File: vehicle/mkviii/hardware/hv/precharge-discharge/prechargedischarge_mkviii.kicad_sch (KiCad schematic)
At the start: 87 parts, among them J2 Conn_01x03_Pin, J3 CONN_pcie_x1, J4 Conn_01x03_Pin, K1 G2RG-2A-X_DC12, K2 3350-4275-126, K3 G2RG-2A-X_DC12, Q1 SSM3K333R, Q2 SSM3K333R, U1 U_GATE_SN74LVC1G02DBVR, U10 SN74LVC1G08DBVR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

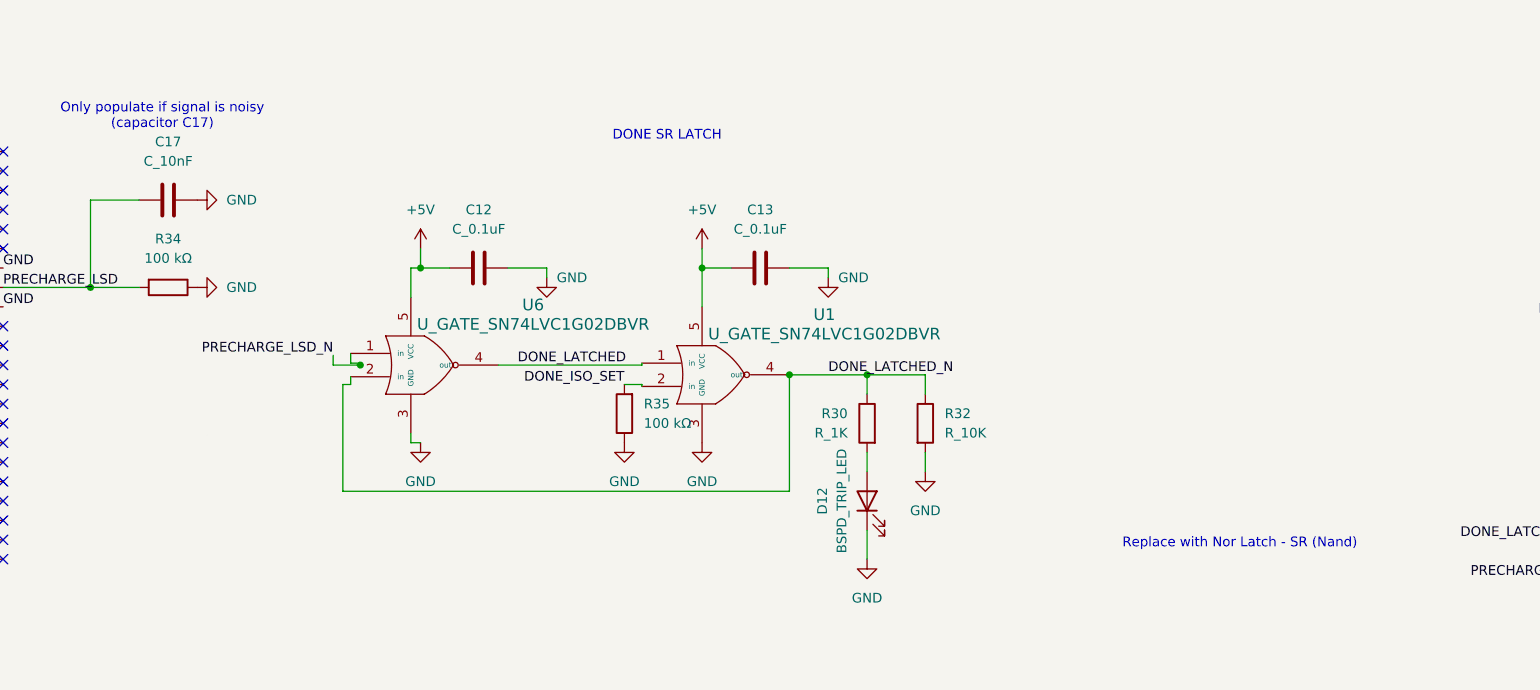
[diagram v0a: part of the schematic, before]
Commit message: Added Production Files; corrected various things in silkscreen and schematics
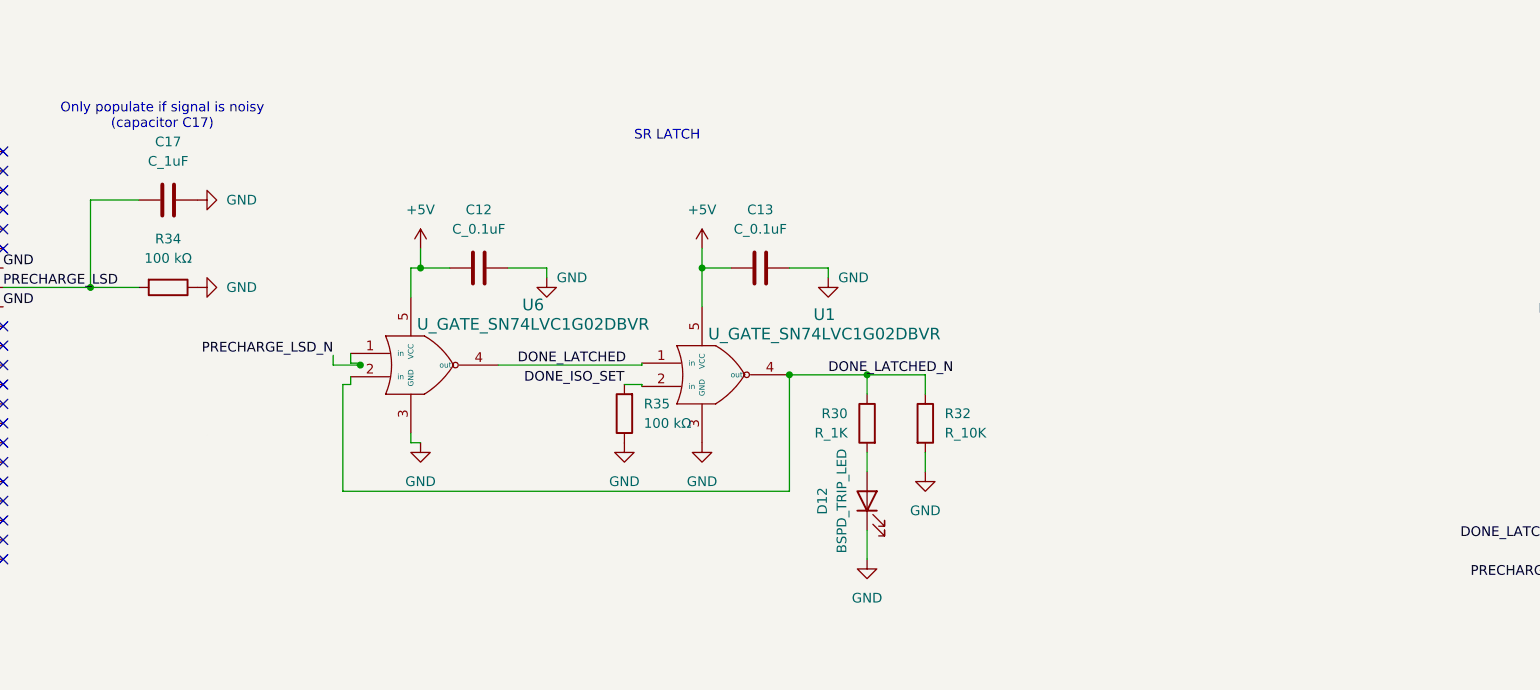
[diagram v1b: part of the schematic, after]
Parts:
- C17: value C_10nF -> C_1uF
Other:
- note added: "SR LATCH"
- note removed: "DONE SR LATCH"
- note removed: "Replace with Nor Latch - SR (Nand)"
- title: (none) -> Precharge-Discharge

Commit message: Prechrarge Discharge - Schematic Organized
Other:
- note added: "HV"
- note added: "LV"
- note added: "Latch Reset"
- note added: "OPTOCOUPLER Isolation"
- note added: "Precharge Completion Comparator"
- note added: "Precharge Done Logic"
- note added: "Precharge Relays"
- note added: "Status Indicator LED"
- note added: "Voltage Divider Network"
- note removed: "OPTOCOUPLER"
- note removed: "Precharge Relay"
- moved on the sheet: C1, C10, C11, C12, C13, C14, C15, C16, C17, C2, C3, C4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

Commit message: Precharge-discharge Renaming for BOM
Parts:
- C11: value C_2.2uF_25V -> C_2.2uF
- C12, C13: value C_0.1uF -> 0.1 µF
- D10, D13: footprint LED_SMD:LED_0805_2012Metric -> OEM:D_0805_2012Metric
- D12: value BSPD_TRIP_LED -> LED_WHITE
- D7, D9: footprint Diode_SMD:D_SMA -> OEM:D_SOD-128
- R1: value 10KR -> R_10K; footprint OEM:R_0603 -> OEM:R_0603_1608Metric
- R11, R5, R7, R8: footprint OEM:R_0603 -> OEM:R_0603_1608Metric
- R24, R27, R30: value R_1K -> 1KR
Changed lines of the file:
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@@
 			)
 		)
-		(property "Footprint" "OEM:R_0603"
+		(property "Footprint" "OEM:R_0603_1608Metric"
 			(at 68.58 191.008 0)
 			(effects
@@
 		)
 		(instances
-			(project "precharge_discharge"
+			(project "prechargedischarge_mkviii"
 				(path "/96f56455-bf31-456c-8371-5b3706690d23"
 					(reference "R8")
@@
 		)
 		(instances
-			(project ""
+			(project "prechargedischarge_mkviii"
 				(path "/96f56455-bf31-456c-8371-5b3706690d23"
 					(reference "U5")
@@
 		)
 		(instances
-			(project "precharge_discharge"
+			(project "prechargedischarge_mkviii"
 				(path "/96f56455-bf31-456c-8371-5b3706690d23"
 					(reference "K1")
@@
 			)
 		)
-		(property "Footprint" "OEM:R_0603"
+		(property "Footprint" "OEM:R_0603_1608Metric"
 			(at 240.03 191.008 90)
 			(effects
@@
 		)
 		(instances
-			(project "precharge_discharge"
+			(project "prechargedischarge_mkviii"
 				(path "/96f56455-bf31-456c-8371-5b3706690d23"
 					(reference "R5")
@@
 			)
 		)
-		(property "Value" "C_0.1uF"
+		(property "Value" "0.1 µF"
 			(at 347.98 54.61 90)
 			(effects
@@
 		)
 		(instances
-			(project ""
+			(project "prechargedischarge_mkviii"
 				(path "/96f56455-bf31-456c-8371-5b3706690d23"
 					(reference "R15")
@@
 		)
 		(instances
-			(project "precharge_discharge"
+			(project "prechargedischarge_mkviii"
 				(path "/96f56455-bf31-456c-8371-5b3706690d23"
 					(reference "J4")
@@
 		)
 		(instances
-			(project "precharge_discharge"
+			(project "prechargedischarge_mkviii"
 				(path "/96f56455-bf31-456c-8371-5b3706690d23"
 					(reference "D1")
@@
 		)
 		(instances
-			(project "precharge_discharge"
+			(project "prechargedischarge_mkviii"
 				(path "/96f56455-bf31-456c-8371-5b3706690d23"
 					(reference "R6")
@@
 		)
 		(instances
-			(project "precharge_discharge"
+			(project "prechargedischarge_mkviii"
 				(path "/96f56455-bf31-456c-8371-5b3706690d23"
 					(reference "#PWR?")
@@
 		)
 		(instances
-			(project "precharge_discharge"
+			(project "prechargedischarge_mkviii"
 				(path "/96f56455-bf31-456c-8371-5b3706690d23"
 					(reference "K2")
@@
 		)
 		(instances
-			(project ""
+			(project "prechargedischarge_mkviii"
 				(path "/96f56455-bf31-456c-8371-5b3706690d23"
 					(reference "R16")
@@
 			)
 		)
-		(property "Value" "BSPD_TRIP_LED"
+		(property "Value" "LED_WHITE"
 			(at 358.648 90.17 0)
 			(effects
@@
 		)
 		(instances
-			(project "precharge_discharge"
+			(project "prechargedischarge_mkviii"
 				(path "/96f56455-bf31-456c-8371-5b3706690d23"
 					(reference "#PWR?")
@@
 		)
 		(instances
-			(project ""
+			(project "prechargedischarge_mkviii"
 				(path "/96f56455-bf31-456c-8371-5b3706690d23"
 					(reference "R13")
@@
 			)
 		)
-		(property "Value" "10KR"
+		(property "Value" "R_10K"
 			(at 92.71 196.8499 0)
 			(effects
@@
 			)
 		)
-		(property "Footprint" "OEM:R_0603"
+		(property "Footprint" "OEM:R_0603_1608Metric"
 			(at 88.392 195.58 90)
 			(effects
@@
 		)
 		(instances
-			(project "precharge_discharge"
+			(project "prechargedischarge_mkviii"
 				(path "/96f56455-bf31-456c-8371-5b3706690d23"
 					(reference "R1")
@@
 		)
 		(instances
-			(project "precharge_discharge"
+			(project "prechargedischarge_mkviii"
 				(path "/96f56455-bf31-456c-8371-5b3706690d23"
 					(reference "R3")
@@
 		)
 		(instances
-			(project ""
+			(project "prechargedischarge_mkviii"
 				(path "/96f56455-bf31-456c-8371-5b3706690d23"
 					(reference "C1")
@@
 		)
 		(instances
-			(project "precharge_discharge"
+			(project "prechargedischarge_mkviii"
 				(path "/96f56455-bf31-456c-8371-5b3706690d23"
 					(reference "D4")
@@
 			)
 		)
-		(property "Footprint" "Diode_SMD:D_SMA"
+		(property "Footprint" "OEM:D_SOD-128"
 			(at 355.6 156.21 0)
 			(effects
@@
 		)
 		(instances
-			(project ""
+			(project "prechargedischarge_mkviii"
 				(path "/96f56455-bf31-456c-8371-5b3706690d23"
 					(reference "#FLG?")
@@
 		)
 		(instances
-			(project ""
+			(project "prechargedischarge_mkviii"
 				(path "/96f56455-bf31-456c-8371-5b3706690d23"
 					(reference "#FLG?")
@@
 		)
 		(instances
-			(project "precharge_discharge"
+			(project "prechargedischarge_mkviii"
 				(path "/96f56455-bf31-456c-8371-5b3706690d23"
 					(reference "#PWR?")
@@
 			)
 		)
-		(property "Footprint" "OEM:R_0603"
+		(property "Footprint" "OEM:R_0603_1608Metric"
 			(at 243.84 169.418 0)
 			(effects
@@
 		)
 		(instances
-			(project "precharge_discharge"
+			(project "prechargedischarge_mkviii"
 				(path "/96f56455-bf31-456c-8371-5b3706690d23"
 					(reference "R7")
@@
 			)
 		)
-		(property "Value" "C_0.1uF"
+		(property "Value" "0.1 µF"
 			(at 311.15 54.61 90)
 			(effects
@@
 		)
 		(instances
-			(project "precharge_discharge"
+			(project "prechargedischarge_mkviii"
 				(path "/96f56455-bf31-456c-8371-5b3706690d23"
 					(reference "Q1")
@@
 		)
 		(instances
-			(project "precharge_discharge"
+			(project "prechargedischarge_mkviii"
 				(path "/96f56455-bf31-456c-8371-5b3706690d23"
 					(reference "D2")
@@
 			)
 		)
-		(property "Footprint" "LED_SMD:LED_0805_2012Metric"
+		(property "Footprint" "OEM:D_0805_2012Metric"
 			(at 430.53 200.66 0)
 			(effects
@@
 		)
 		(instances
-			(project ""
+			(project "prechargedischarge_mkviii"
 				(path "/96f56455-bf31-456c-8371-5b3706690d23"
 					(reference "#FLG?")
@@
 		)
 		(instances
-			(project ""
+			(project "prechargedischarge_mkviii"
 				(path "/96f56455-bf31-456c-8371-5b3706690d23"
 					(reference "J2")
@@
 		)
 		(instances
-			(project ""
+			(project "prechargedischarge_mkviii"
 				(path "/96f56455-bf31-456c-8371-5b3706690d23"
 					(reference "R14")
@@
 		)
 		(instances
-			(project ""
+			(project "prechargedischarge_mkviii"
 				(path "/96f56455-bf31-456c-8371-5b3706690d23"
 					(reference "R31")
@@
 		)
 		(instances
-			(project "precharge_discharge"
+			(project "prechargedischarge_mkviii"
 				(path "/96f56455-bf31-456c-8371-5b3706690d23"
 					(reference "D3")
@@
 		)
 		(instances
-			(project ""
+			(project "prechargedischarge_mkviii"
 				(path "/96f56455-bf31-456c-8371-5b3706690d23"
 					(reference "U7")
@@
 			)
 		)
-		(property "Footprint" "OEM:R_0603"
+		(property "Footprint" "OEM:R_0603_1608Metric"
 			(at 158.75 189.738 0)
 			(effects
@@
 			)
 		)
-		(property "Value" "C_2.2uF_25V"
+		(property "Value" "C_2.2uF"
 			(at 182.88 203.1999 0)
 			(effects
@@
 		)
 		(instances
-			(project ""
+			(project "prechargedischarge_mkviii"
 				(path "/96f56455-bf31-456c-8371-5b3706690d23"
 					(reference "C11")
@@
 		)
 		(instances
-			(project "precharge_discharge"
+			(project "prechargedischarge_mkviii"
 				(path "/96f56455-bf31-456c-8371-5b3706690d23"
 					(reference "J3")
@@
 		)
 		(instances
-			(project "precharge_discharge"
+			(project "prechargedischarge_mkviii"
 				(path "/96f56455-bf31-456c-8371-5b3706690d23"
 					(reference "R2")
@@
 			)
 		)
-		(property "Footprint" "LED_SMD:LED_0805_2012Metric"
+		(property "Footprint" "OEM:D_0805_2012Metric"
 			(at 245.11 128.27 0)
 			(effects
@@
 		)
 		(instances
-			(project ""
+			(project "prechargedischarge_mkviii"
 				(path "/96f56455-bf31-456c-8371-5b3706690d23"
 					(reference "D11")
@@
 		)
 		(instances
-			(project "precharge_discharge"
+			(project "prechargedischarge_mkviii"
 				(path "/96f56455-bf31-456c-8371-5b3706690d23"
 					(reference "#PWR?")
@@
 		)
 		(instances
-			(project ""
+			(project "prechargedischarge_mkviii"
 				(path "/96f56455-bf31-456c-8371-5b3706690d23"
 					(reference "#FLG?")
@@
 			)
 		)
-		(property "Value" "R_1K"
+		(property "Value" "1KR"
 			(at 236.093 126.492 0)
 			(effects
@@
 			)
 		)
-		(property "Value" "R_1K"
+		(property "Value" "1KR"
 			(at 359.41 81.2799 0)
 			(effects
@@
 		)
 		(instances
-			(project ""
+			(project "prechargedischarge_mkviii"
 				(path "/96f56455-bf31-456c-8371-5b3706690d23"
 					(reference "U8")
@@
 		)
 		(instances
-			(project ""
+			(project "prechargedischarge_mkviii"
 				(path "/96f56455-bf31-456c-8371-5b3706690d23"
 					(reference "U2")
@@
 		)
 		(instances
-			(project "precharge_discharge"
+			(project "prechargedischarge_mkviii"
 				(path "/96f56455-bf31-456c-8371-5b3706690d23"
 					(reference "#PWR?")
@@
 			)
 		)
-		(property "Footprint" "Diode_SMD:D_SMA"
+		(property "Footprint" "OEM:D_SOD-128"
 			(at 387.35 156.21 0)
 			(effects
@@
 		)
 		(instances
-			(project ""
+			(project "prechargedischarge_mkviii"
 				(path "/96f56455-bf31-456c-8371-5b3706690d23"
 					(reference "#PWR?")
@@
 		)
 		(instances
-			(project "precharge_discharge"
+			(project "prechargedischarge_mkviii"
 				(path "/96f56455-bf31-456c-8371-5b3706690d23"
 					(reference "R4")
@@
 			)
 		)
-		(property "Value" "R_1K"
+		(property "Value" "1KR"
 			(at 439.928 195.453 0)
 			(effects
